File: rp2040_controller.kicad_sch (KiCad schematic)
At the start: 34 parts, among them J1 Conn_01x12, J2 Conn_01x15, J3 Conn_01x12, J4 Conn_01x05, J5 Conn_01x02, J6 Conn_01x02, U1 RP2040, U2 AP2112K-3.3, U3 W25Q64JV, Y1 XYDBPCNANF-12MHZ

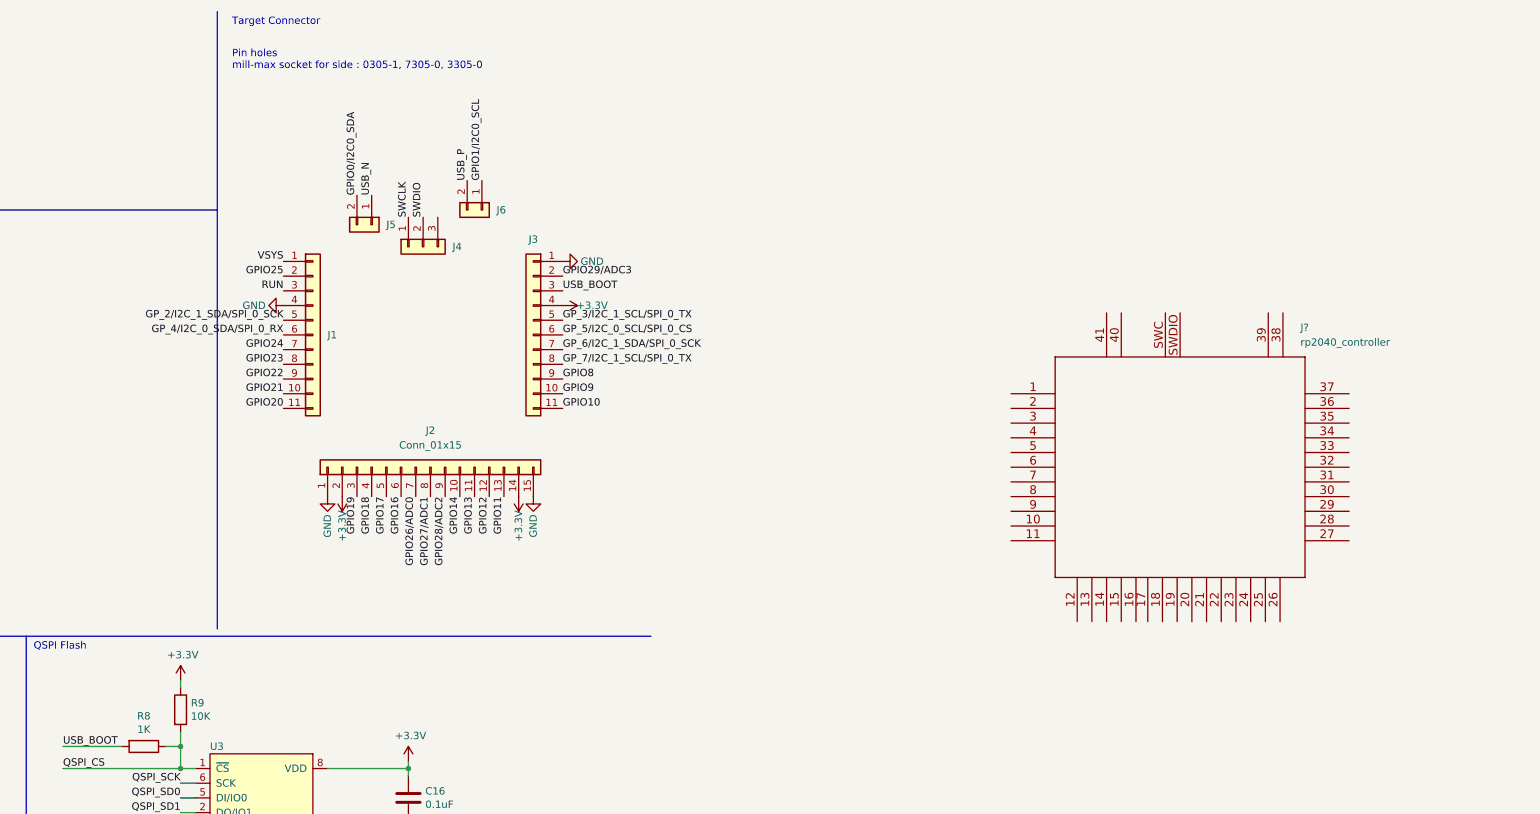
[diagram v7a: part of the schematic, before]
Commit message: top&bottom connect
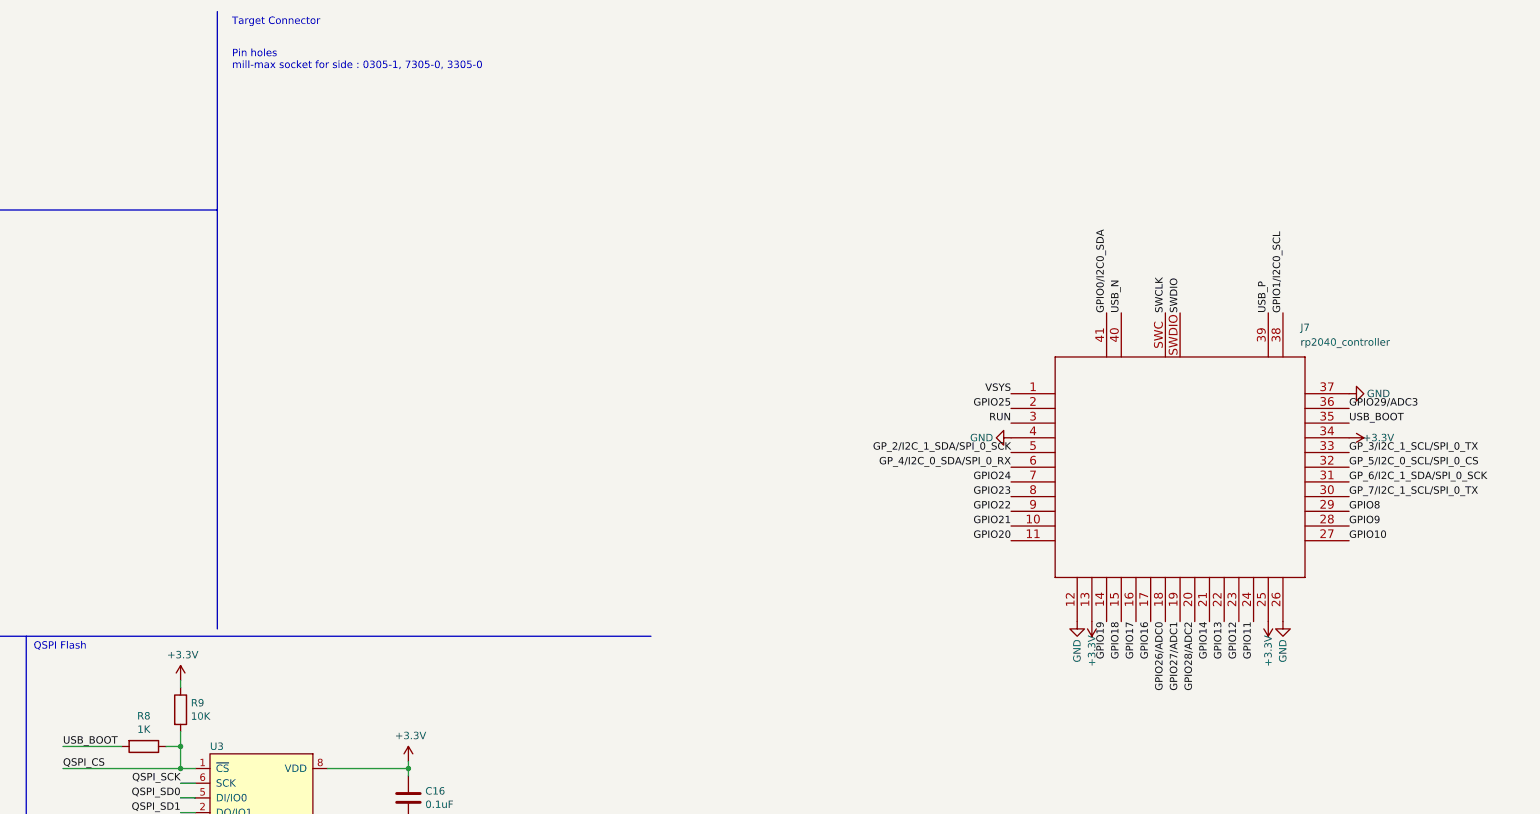
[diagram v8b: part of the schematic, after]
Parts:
- removed J1, J3: Conn_01x12, ec_parts:PinHeader_1x12_P2.54mm_Vertical, symbol Connector_Generic:Conn_01x11
- removed J2: Conn_01x15, ec_parts:PinHeader_1x15_P1.27mm_Vertical, symbol Connector_Generic:Conn_01x15
- removed J4: Conn_01x05, ec_parts:TestPinHeader_1x03_P1.27mm_Vertical, symbol Connector_Generic:Conn_01x03
- removed J5, J6: Conn_01x02, Connector_PinHeader_2.54mm:PinHeader_1x02_P2.54mm_Vertical, symbol Connector_Generic:Conn_01x02
- J7: renamed from J?; footprint ec_parts:ec_pad_1x15_P1.27mm -> ec_parts:rp2040_controller
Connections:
- net +3V3: now also J7.13 (GPIO10), J7.25 (SWDIO), J7.34 (GPIO22)
- net GND: now also J7.12 (GPIO9), J7.26 (RUN), J7.37 (GPIO25), J7.4 (GPIO2)
- net GPIO0/I2C0_SDA: now also J7.41 (GPIO29/ADC3)
- net GPIO10: now also J7.27 (GPIO16)
- net GPIO11: now also J7.24 (SWCLK)
- net GPIO12: now also J7.23 (DVDD)
- net GPIO13: now also J7.22 (IOVDD)
- net GPIO14: now also J7.21 (XOUT)
- net GPIO16: now also J7.17 (GPIO14)
- net GPIO17: now also J7.16 (GPIO13)
- net GPIO18: now also J7.15 (GPIO12)
- net GPIO19: now also J7.14 (GPIO11)
- net GPIO1/I2C0_SCL: now also J7.38 (GPIO26/ADC0)
- net GPIO20: now also J7.11 (GPIO8)
- net GPIO21: now also J7.10 (IOVDD)
- net GPIO22: now also J7.9 (GPIO7)
- net GPIO23: now also J7.8 (GPIO6)
- net GPIO24: now also J7.7 (GPIO5)
- net GPIO25: now also J7.2 (GPIO0)
- net GPIO26/ADC0: now also J7.18 (GPIO15)
- net GPIO27/ADC1: now also J7.19 (TESTEN)
- net GPIO28/ADC2: now also J7.20 (XIN)
- net GPIO29/ADC3: now also J7.36 (GPIO24)
- net GPIO8: now also J7.29 (GPIO18)
- net GPIO9: now also J7.28 (GPIO17)
- net GP_2/I2C_1_SDA/SPI_0_SCK: now also J7.5 (GPIO3)
- net GP_3/I2C_1_SCL/SPI_0_TX : now also J7.33 (IOVDD)
- net GP_4/I2C_0_SDA/SPI_0_RX: now also J7.6 (GPIO4)
- net GP_5/I2C_0_SCL/SPI_0_CS: now also J7.32 (GPIO21)
- net GP_6/I2C_1_SDA/SPI_0_SCK: now also J7.31 (GPIO20)
- net GP_7/I2C_1_SCL/SPI_0_TX: now also J7.30 (GPIO19)
- net RUN: now also J7.3 (GPIO1)
- net SWCLK: now also J7.SWC
- net SWDIO: now also J7.SWDIO
- net USB_BOOT: now also J7.35 (GPIO23)
- net USB_N: now also J7.40 (GPIO28/ADC2)
- net USB_P: now also J7.39 (GPIO27/ADC1)
- net VSYS: now also J7.1 (IOVDD)
